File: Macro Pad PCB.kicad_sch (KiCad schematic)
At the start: 40 parts, among them J1 Debug, Q1 DMG1012T, U1 RP2040, U2 W25Q16JVSNIQ, U3 MIC5365-3.3YC5-TR, U4 IP4234CZ6, Y2 12 MHz

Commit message: Routing Continued
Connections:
- net +3.3V: no longer U1.10 (IOVDD)
- net d2N: now reaches R14.2, U4.1 (ESD_CH1)
- net dN: now reaches U4.3 (ESD_CH1.2), USB1.5 (DN2), USB1.7 (DN1)
- net dP: now reaches U4.4 (ESD_CH2.2), USB1.6 (DP1), USB1.8 (DP2)
- net d2P: now reaches R13.2, U4.6 (ESD_CH2)
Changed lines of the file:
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@@
     (stroke (width 0) (type default) (color 0 0 0 0))
   )
-  (wire (pts (xy 215.265 46.99) (xy 234.315 46.99))
+  (wire (pts (xy 234.315 66.04) (xy 234.315 46.99))
     (stroke (width 0) (type default) (color 0 0 0 0))
   )
@@
     )
   )
+  (global_label "d2N" (shape input) (at 133.985 90.805 90) (fields_autoplaced)
+    (effects (font (size 1.27 1.27)) (justify left))
+    (property "Intersheet References" "${INTERSHEET_REFS}" (id 0) (at 133.9056 84.7029 90)
+      (effects (font (size 1.27 1.27)) (justify left) hide)
+    )
+  )
   (global_label "RUN" (shape input) (at 177.165 124.46 180) (fields_autoplaced)
     (effects (font (size 1.27 1.27)) (justify right))
@@
     )
   )
+  (global_label "d2P" (shape input) (at 137.16 92.075 270) (fields_autoplaced)
+    (effects (font (size 1.27 1.27)) (justify right))
+    (property "Intersheet References" "${INTERSHEET_REFS}" (id 0) (at 137.0806 98.1167 90)
+      (effects (font (size 1.27 1.27)) (justify right) hide)
+    )
+  )
   (global_label "RUN" (shape input) (at 31.75 149.86 180) (fields_autoplaced)
     (effects (font (size 1.27 1.27)) (justify right))
@@
     )
   )
+  (global_label "dN" (shape input) (at 118.11 88.9 270) (fields_autoplaced)
+    (effects (font (size 1.27 1.27)) (justify right))
+    (property "Intersheet References" "${INTERSHEET_REFS}" (id 0) (at 118.0306 93.7926 90)
+      (effects (font (size 1.27 1.27)) (justify right) hide)
+    )
+  )
   (global_label "QSPI_SD2" (shape input) (at 177.165 81.28 180) (fields_autoplaced)
     (effects (font (size 1.27 1.27)) (justify right))
@@
     )
   )
+  (global_label "dP" (shape input) (at 120.65 93.345 270) (fields_autoplaced)
+    (effects (font (size 1.27 1.27)) (justify right))
+    (property "Intersheet References" "${INTERSHEET_REFS}" (id 0) (at 120.5706 98.1771 90)
+      (effects (font (size 1.27 1.27)) (justify right) hide)
+    )
+  )

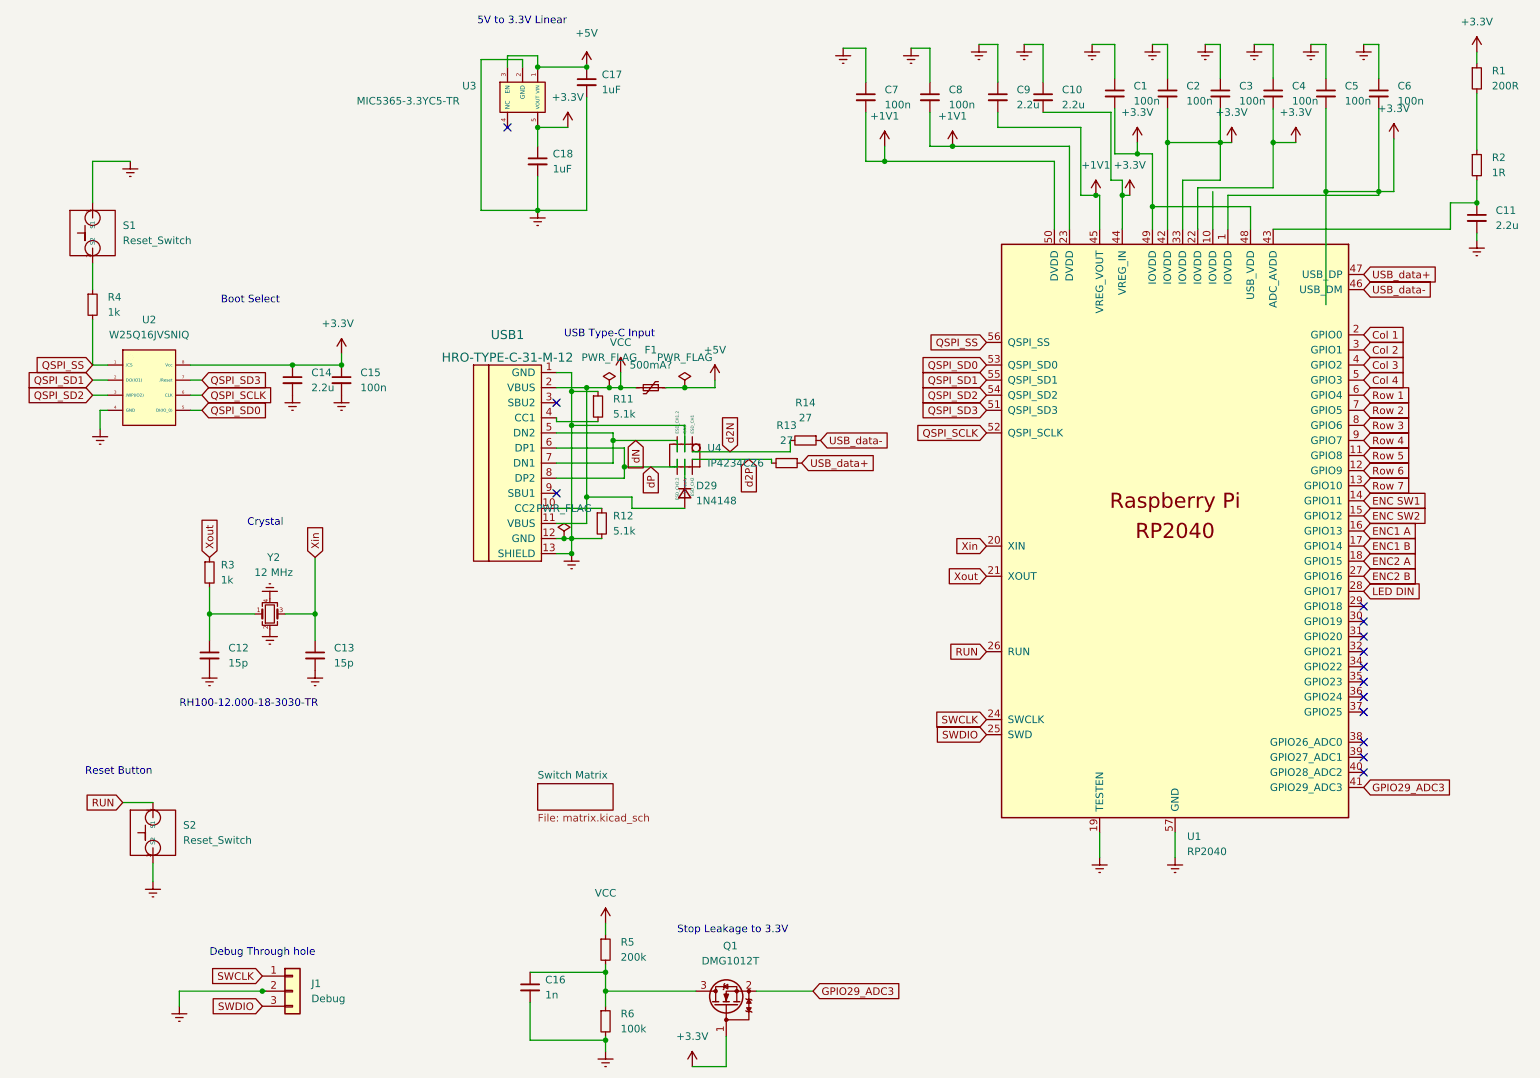
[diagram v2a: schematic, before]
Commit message: Routing Finished and ESD Protection Enhanced
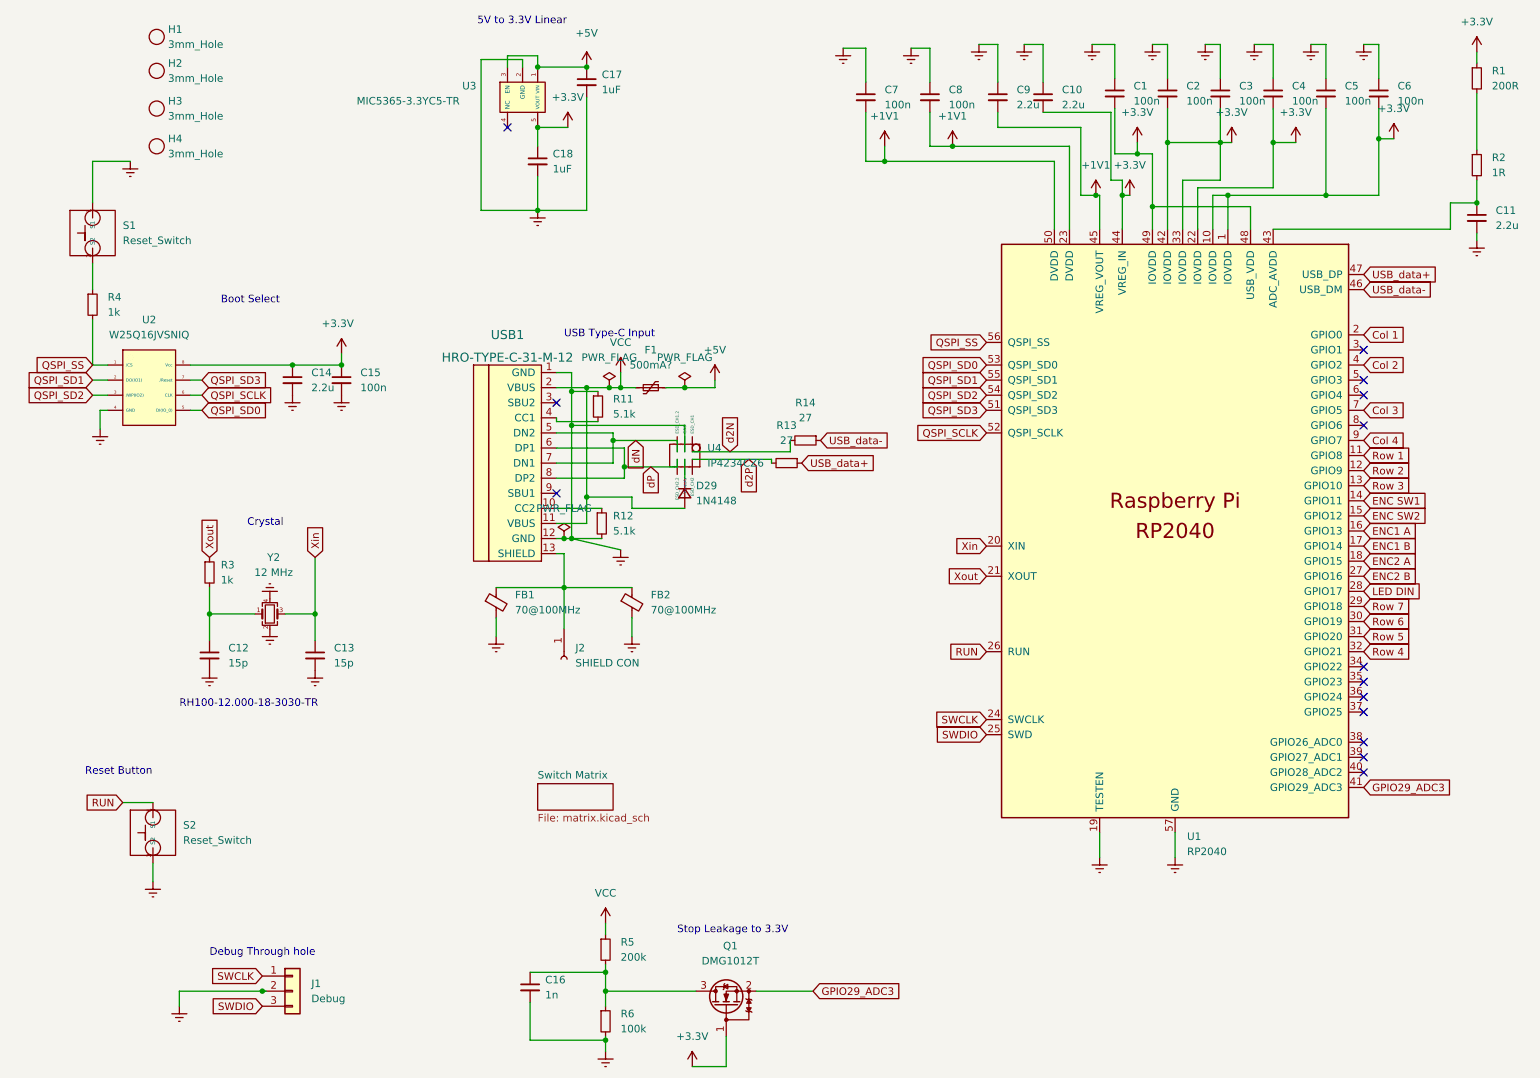
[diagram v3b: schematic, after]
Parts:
- added FB1, FB2: 70@100MHz, Inductor_SMD:L_0603_1608Metric_Pad1.05x0.95mm_HandSolder, symbol Device:FerriteBead_Small
- added H1, H2, H3, H4: 3mm_Hole, Reset Switch:3mm Hole, symbol Reset Switch:3mm_Hole
- added J2: SHIELD CON, Connector_PinHeader_2.54mm:PinHeader_1x01_P2.54mm_Vertical, symbol Connector:Conn_01x01_Female
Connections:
- net +3.3V: now also U1.10 (IOVDD)
- net Col 2: now also U1.4 (GPIO2); no longer U1.3 (GPIO1)
- net Col 3: now also U1.7 (GPIO5); no longer U1.4 (GPIO2)
- net Col 4: now also U1.9 (GPIO7); no longer U1.5 (GPIO3)
- net Earth: now also FB1.2, FB2.2; no longer USB1.13 (SHIELD)
- net Row 1: now also U1.11 (GPIO8); no longer U1.6 (GPIO4)
- net Row 2: now also U1.12 (GPIO9); no longer U1.7 (GPIO5)
- net Row 3: now also U1.13 (GPIO10); no longer U1.8 (GPIO6)
- net Row 4: now also U1.32 (GPIO21); no longer U1.9 (GPIO7)
- net Row 5: now also U1.31 (GPIO20); no longer U1.11 (GPIO8)
- net Row 6: now also U1.30 (GPIO19); no longer U1.12 (GPIO9)
- net Row 7: now also U1.29 (GPIO18); no longer U1.13 (GPIO10)
- new net: FB1.1, FB2.1, J2.1 (Pin_1), USB1.13 (SHIELD)
